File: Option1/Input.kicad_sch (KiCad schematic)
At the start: 3 parts, among them J1 Conn_02x07_Odd_Even, U1_I/O_Old1 1989780, U2_CAN1 1989780

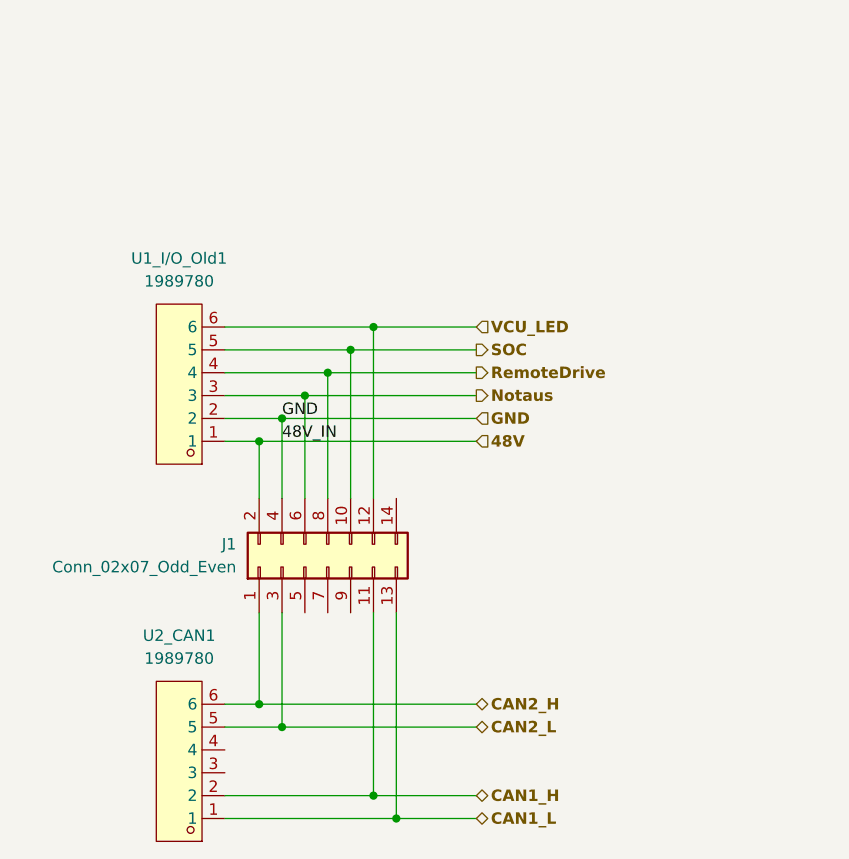
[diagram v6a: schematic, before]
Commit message: funkempfänger mit Beschaltung zu Layout hinzugefügt, SPI und I2C teilnehmer geroutet, Löcher hinzugefügt, Stecker platziert
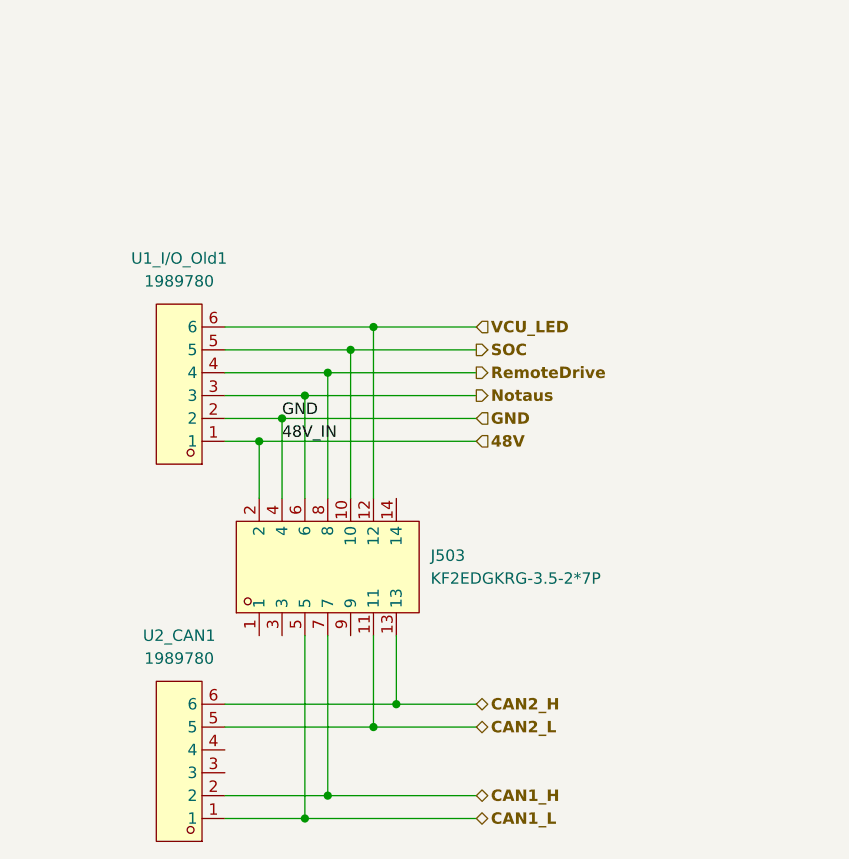
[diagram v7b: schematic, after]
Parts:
- removed J1: Conn_02x07_Odd_Even, Connector_PinHeader_2.54mm:PinHeader_2x07_P2.54mm_Vertical, symbol Connector_Generic:Conn_02x07_Odd_Even
- added J503: KF2EDGKRG-3.5-2*7P, easyeda2kicad:CONN-TH_14P-P3.50_KEFA_KF2EDGKRG-3.5-2X7P, symbol easyeda2kicad:KF2EDGKRG-3.5-2*7P
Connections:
- net 48V: now also J503.2, J503.4
- net CAN1_H: now also J503.7
- net CAN1_L: now also J503.5
- net CAN2_H: now also J503.13
- net CAN2_L: now also J503.11
- net Notaus: now also J503.6
- net RemoteDrive: now also J503.8
- net SOC: now also J503.10
- net VCU_LED: now also J503.12
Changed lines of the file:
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@@
-	)
-	(junction
-		(at 33.02 93.98)
-		(diameter 0)
-		(color 0 0 0 0)
 	)
 	(junction
@@
 	)
 	(junction
-		(at 30.48 91.44)
-		(diameter 0)
-		(color 0 0 0 0)
-	)
-	(junction
 		(at 43.18 49.53)
 		(diameter 0)
@@
 	)
 	(junction
-		(at 43.18 101.6)
+		(at 38.1 101.6)
+		(diameter 0)
+		(color 0 0 0 0)
+	)
+	(junction
+		(at 35.56 104.14)
 		(diameter 0)
 		(color 0 0 0 0)
@@
 	)
 	(junction
+		(at 43.18 93.98)
+		(diameter 0)
+		(color 0 0 0 0)
+	)
+	(junction
 		(at 35.56 57.15)
 		(diameter 0)
@@
 	)
 	(junction
-		(at 45.72 104.14)
+		(at 45.72 91.44)
 		(diameter 0)
 		(color 0 0 0 0)
@@
 	(wire
 		(pts
-			(xy 45.72 81.28) (xy 45.72 104.14)
-		)
-		(stroke
-			(width 0)
-			(type default)
-		)
-	)
-	(wire
-		(pts
-			(xy 45.72 104.14) (xy 54.61 104.14)
-		)
-		(stroke
-			(width 0)
-			(type default)
-		)
-	)
-	(wire
-		(pts
-			(xy 26.67 93.98) (xy 33.02 93.98)
-		)
-		(stroke
-			(width 0)
-			(type default)
-		)
-	)
-	(wire
-		(pts
-			(xy 43.18 81.28) (xy 43.18 101.6)
-		)
-		(stroke
-			(width 0)
-			(type default)
-		)
-	)
-	(wire
-		(pts
-			(xy 30.48 81.28) (xy 30.48 91.44)
+			(xy 35.56 104.14) (xy 54.61 104.14)
+		)
+		(stroke
+			(width 0)
+			(type default)
+		)
+	)
+	(wire
+		(pts
+			(xy 26.67 104.14) (xy 35.56 104.14)
+		)
+		(stroke
+			(width 0)
+			(type default)
+		)
+	)
+	(wire
+		(pts
+			(xy 45.72 83.82) (xy 45.72 91.44)
+		)
+		(stroke
+			(width 0)
+			(type default)
+		)
+	)
+	(wire
+		(pts
+			(xy 26.67 93.98) (xy 43.18 93.98)
 		)
 		(stroke
@@
 	(wire
 		(pts
+			(xy 43.18 93.98) (xy 54.61 93.98)
+		)
+		(stroke
+			(width 0)
+			(type default)
+		)
+	)
+	(wire
+		(pts
 			(xy 35.56 57.15) (xy 54.61 57.15)
 		)
@@
 	(wire
 		(pts
-			(xy 26.67 101.6) (xy 43.18 101.6)
+			(xy 26.67 101.6) (xy 38.1 101.6)
 		)
 		(stroke
@@
 	(wire
 		(pts
+			(xy 38.1 101.6) (xy 54.61 101.6)
+		)
+		(stroke
+			(width 0)
+			(type default)
+		)
+	)
+	(wire
+		(pts
 			(xy 40.64 52.07) (xy 40.64 68.58)
 		)
@@
 	(wire
 		(pts
+			(xy 45.72 91.44) (xy 54.61 91.44)
+		)
+		(stroke
+			(width 0)
+			(type default)
+		)
+	)
+	(wire
+		(pts
 			(xy 38.1 54.61) (xy 38.1 68.58)
 		)
@@
 	(wire
 		(pts
-			(xy 54.61 101.6) (xy 43.18 101.6)
-		)
-		(stroke
-			(width 0)
-			(type default)
-		)
-	)
-	(wire
-		(pts
-			(xy 33.02 93.98) (xy 54.61 93.98)
-		)
-		(stroke
-			(width 0)
-			(type default)
-		)
-	)
-	(wire
-		(pts
-			(xy 26.67 91.44) (xy 30.48 91.44)
-		)
-		(stroke
-			(width 0)
-			(type default)
-		)
-	)
-	(wire
-		(pts
-			(xy 33.02 81.28) (xy 33.02 93.98)
-		)
-		(stroke
-			(width 0)
-			(type default)
-		)
-	)
-	(wire
-		(pts
-			(xy 30.48 91.44) (xy 54.61 91.44)
+			(xy 38.1 83.82) (xy 38.1 101.6)
+		)
+		(stroke
+			(width 0)
+			(type default)
+		)
+	)
+	(wire
+		(pts
+			(xy 26.67 91.44) (xy 45.72 91.44)
+		)
+		(stroke
+			(width 0)
+			(type default)
+		)
+	)
+	(wire
+		(pts
+			(xy 35.56 83.82) (xy 35.56 104.14)
 		)
 		(stroke
@@
 	(wire
 		(pts
+			(xy 43.18 83.82) (xy 43.18 93.98)
+		)
+		(stroke
+			(width 0)
+			(type default)
+		)
+	)
+	(wire
+		(pts
 			(xy 30.48 62.23) (xy 30.48 68.58)
-		)
-		(stroke
-			(width 0)
-			(type default)
-		)
-	)
-	(wire
-		(pts
-			(xy 26.67 104.14) (xy 45.72 104.14)
 		)
 		(stroke
@@
 	)
 	(symbol
-		(lib_id "Connector_Generic:Conn_02x07_Odd_Even")
+		(lib_id "easyeda2kicad:KF2EDGKRG-3.5-2*7P")
 		(at 38.1 76.2 90)
 		(unit 1)
@@
 		(dnp no)
 		(fields_autoplaced yes)
-		(property "Reference" "J1"
-			(at 27.94 73.6599 90)
-			(effects
-				(font
-					(size 1.27 1.27)
-				)
-				(justify left)
-			)
-		)
-		(property "Value" "Conn_02x07_Odd_Even"
-			(at 27.94 76.1999 90)
-			(effects
-				(font
-					(size 1.27 1.27)
-				)
-				(justify left)
-			)
-		)
-		(property "Footprint" "Connector_PinHeader_2.54mm:PinHeader_2x07_P2.54mm_Vertical"
+		(property "Reference" "J503"
+			(at 49.53 74.9299 90)
+			(effects
+				(font
+					(size 1.27 1.27)
+				)
+				(justify right)
+			)
+		)
+		(property "Value" "KF2EDGKRG-3.5-2*7P"
+			(at 49.53 77.4699 90)
+			(effects
+				(font
+					(size 1.27 1.27)
+				)
+				(justify right)
+			)
+		)
+		(property "Footprint" "easyeda2kicad:CONN-TH_14P-P3.50_KEFA_KF2EDGKRG-3.5-2X7P"
+			(at 53.34 76.2 0)
+			(effects
+				(font
+					(size 1.27 1.27)
+				)
+				(hide yes)
+			)
+		)
+		(property "Datasheet" ""
 			(at 38.1 76.2 0)
 			(effects
@@
 			)
 		)
-		(property "Datasheet" "~"
+		(property "Description" ""
 			(at 38.1 76.2 0)
 			(effects
@@
 			)
 		)
-		(property "Description" "Generic connector, double row, 02x07, odd/even pin numbering scheme (row 1 odd numbers, row 2 even numbers), script generated (kicad-library-utils/schlib/autogen/connector/)"
-			(at 38.1 76.2 0)
+		(property "LCSC Part" "C2923184"
+			(at 55.88 76.2 0)
 			(effects
 				(font
@@
 		(pin "13"
 		)
+		(pin "14"
+		)
+		(pin "4"
+		)
+		(pin "5"
+		)
+		(pin "12"
+		)
+		(pin "3"
+		)
+		(pin "9"
+		)
+		(pin "11"
+		)
+		(pin "2"
+		)
+		(pin "8"
+		)
+		(pin "10"
+		)
+		(pin "1"
+		)
 		(pin "7"
 		)
-		(pin "4"
-		)
-		(pin "8"
-		)
-		(pin "10"
-		)
-		(pin "1"
-		)
 		(pin "6"
-		)
-		(pin "3"
-		)
-		(pin "5"
-		)
-		(pin "2"
-		)
-		(pin "12"
-		)
-		(pin "9"
-		)
-		(pin "14"
-		)
-		(pin "11"
 		)
 		(instances
 			(project ""
 				(path "/b9e5f262-9648-4b79-bdd1-af888b822329/f9f0c67f-dd50-4740-b345-6512cc3de02a"
-					(reference "J1")
+					(reference "J503")
 					(unit 1)
 				)

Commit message: Layout komplett bis auf RFID Leiste und 3V3 Erzeugung Display
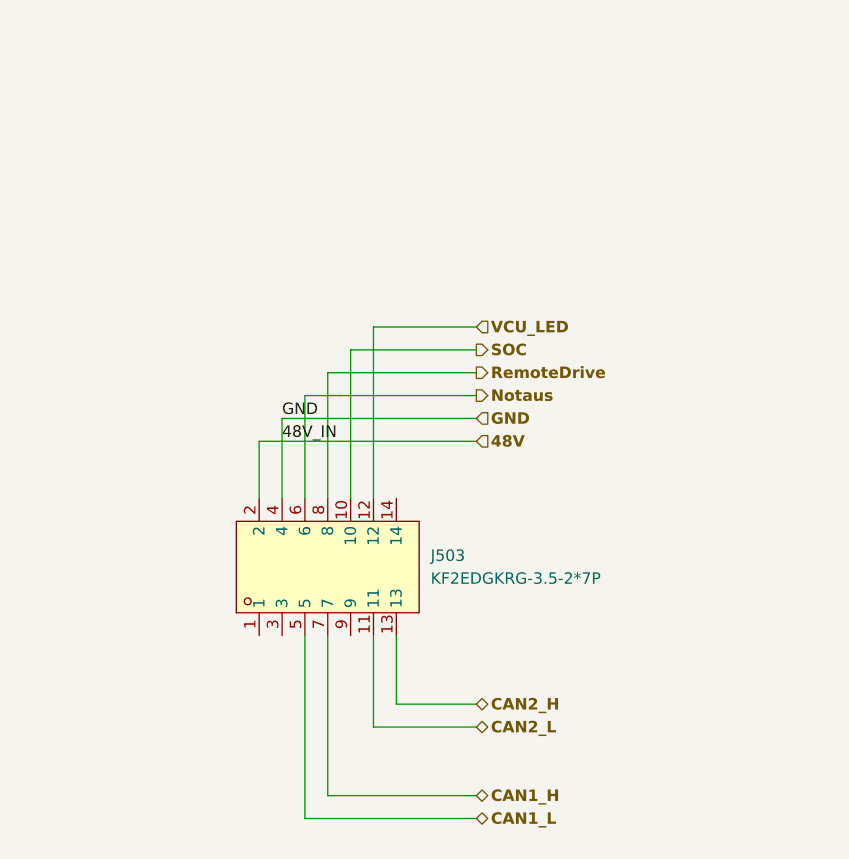
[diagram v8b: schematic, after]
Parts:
- removed U1_I/O_Old1, U2_CAN1: 1989780, easyeda2kicad:CONN-TH_6P-P2.50_1989780, symbol EasyEda2KiCad:1989780
